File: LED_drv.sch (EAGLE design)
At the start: 69 parts, among them IC1 LM3409, IC2 LM393D, Q2 IPD50R380, T1 IRLR9343PBF, T2 BCX56, T4 BT169, T5 BT169, T6 TLP266J

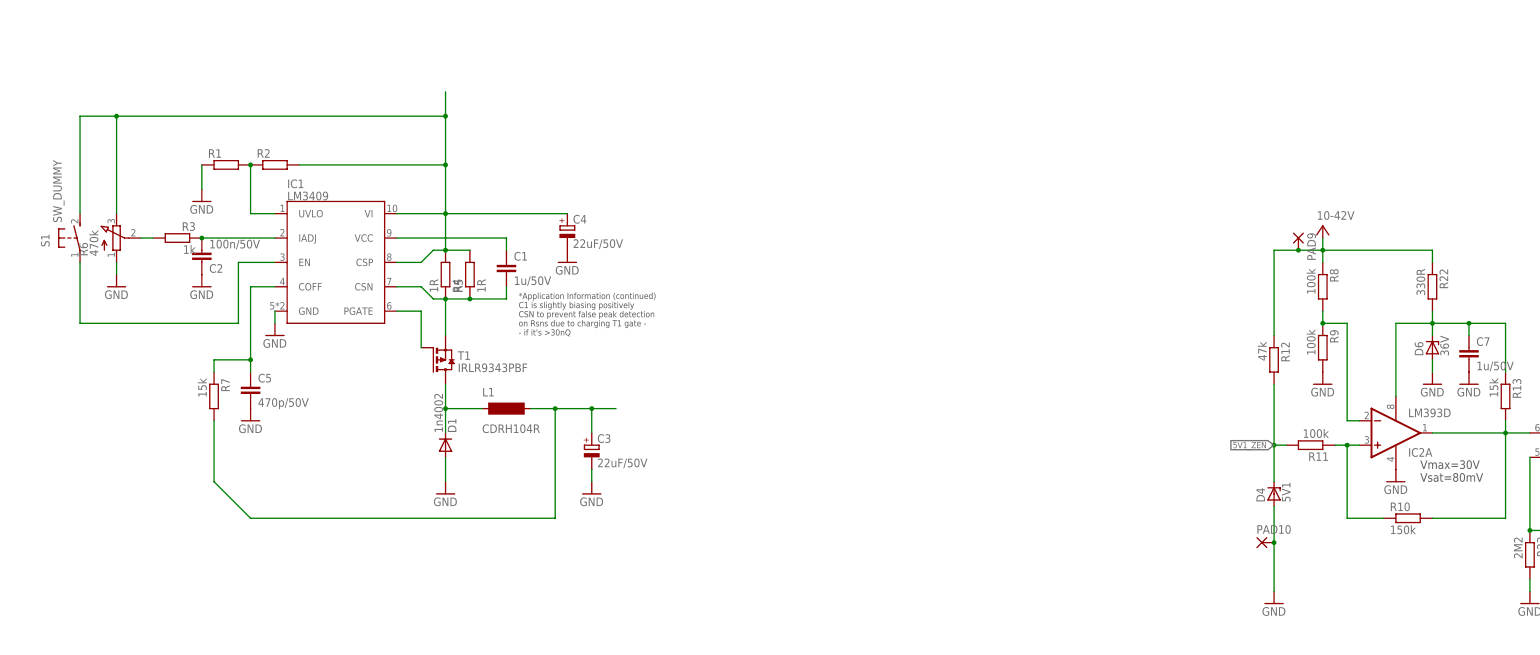
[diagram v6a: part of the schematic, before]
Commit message: PCB layout complete
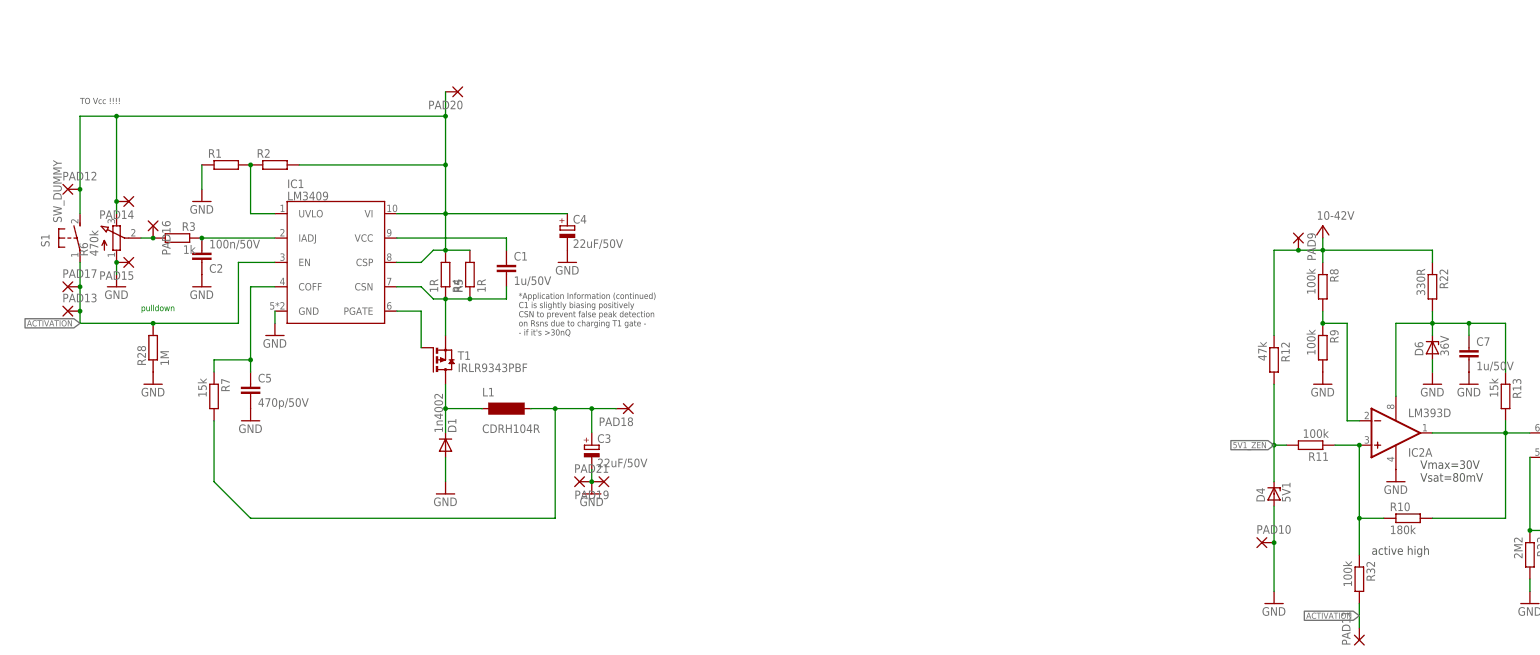
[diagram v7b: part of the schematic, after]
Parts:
- added PAD11, PAD12, PAD13, PAD14, PAD15, PAD16, PAD17, PAD18, PAD19, PAD20, PAD21: (no value), wirepad:SMD2
- added R28: 1M, rcl:R-EU_R0805
- added R32: 100k, resistor:R-EU_R0805
- R1, R2, R7: device rcl:R-EU_R0805 -> rcl:R-EU_R1206
- R10: value 150k -> 180k; device resistor:R-EU_R0805 -> rcl:R-EU_R1206
- R27, R9: device resistor:R-EU_R0805 -> rcl:R-EU_R1206
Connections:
- removed net N$11: IC1.EN, S1.P
- removed net N$20: IC2A.+IN, R10.1, R11.1
- new net ACTIVATION: IC1.EN, PAD11.P, PAD13.P, PAD17.P, R28.2, R32.2, S1.P
- new net EER: IC2A.+IN, R10.1, R11.1, R32.1
- net GND: now also PAD15.P, PAD19.P, PAD21.P, R28.1
- net N$10: now also PAD18.P
- net N$2: now also PAD12.P, PAD14.P, PAD20.P
- net N$8: now also PAD16.P
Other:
- note added: "TO Vcc !!!!"
- note added: "active high"
- note added: "pulldown"
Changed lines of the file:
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@@
 <parts>
 <part name="IC1" library="TI" deviceset="LM3409" device=""/>
-<part name="R1" library="rcl" deviceset="R-EU_" device="R0805"/>
-<part name="R2" library="rcl" deviceset="R-EU_" device="R0805"/>
+<part name="R1" library="rcl" deviceset="R-EU_" device="R1206"/>
+<part name="R2" library="rcl" deviceset="R-EU_" device="R1206"/>
 <part name="GND1" library="supply1" deviceset="GND" device=""/>
 <part name="GND2" library="supply1" deviceset="GND" device=""/>
@@
 <part name="S1" library="switch-omron" deviceset="SW_DUMMY" device=""/>
 <part name="C5" library="rcl" deviceset="C-EU" device="C1206" value="470p/50V"/>
-<part name="R7" library="rcl" deviceset="R-EU_" device="R0805" value="15k"/>
+<part name="R7" library="rcl" deviceset="R-EU_" device="R1206" value="15k"/>
 <part name="GND8" library="supply1" deviceset="GND" device=""/>
 <part name="IC2" library="linear" deviceset="LM393" device="D"/>
 <part name="R8" library="resistor" deviceset="R-EU_" device="R0805" value="100k"/>
-<part name="R9" library="resistor" deviceset="R-EU_" device="R0805" value="100k"/>
-<part name="R10" library="resistor" deviceset="R-EU_" device="R0805" value="150k"/>
+<part name="R9" library="rcl" deviceset="R-EU_" device="R1206" value="100k"/>
+<part name="R10" library="rcl" deviceset="R-EU_" device="R1206" value="180k"/>
 <part name="R11" library="resistor" deviceset="R-EU_" device="R0805" value="100k"/>
 <part name="R12" library="resistor" deviceset="R-EU_" device="R0805" value="47k"/>
@@
 <part name="PAD9" library="wirepad" deviceset="SMD2" device=""/>
 <part name="PAD10" library="wirepad" deviceset="SMD2" device=""/>
-<part name="R27" library="resistor" deviceset="R-EU_" device="R0805" value="0"/>
+<part name="R27" library="rcl" deviceset="R-EU_" device="R1206" value="0"/>
+<part name="R28" library="rcl" deviceset="R-EU_" device="R0805" value="1M"/>
+<part name="GND16" library="supply1" deviceset="GND" device=""/>
+<part name="PAD11" library="wirepad" deviceset="SMD2" device=""/>
+<part name="R32" library="resistor" deviceset="R-EU_" device="R0805" value="100k"/>
+<part name="PAD12" library="wirepad" deviceset="SMD2" device=""/>
+<part name="PAD13" library="wirepad" deviceset="SMD2" device=""/>
+<part name="PAD14" library="wirepad" deviceset="SMD2" device=""/>
+<part name="PAD15" library="wirepad" deviceset="SMD2" device=""/>
+<part name="PAD16" library="wirepad" deviceset="SMD2" device=""/>
+<part name="PAD17" library="wirepad" deviceset="SMD2" device=""/>
+<part name="PAD18" library="wirepad" deviceset="SMD2" device=""/>
+<part name="PAD19" library="wirepad" deviceset="SMD2" device=""/>
+<part name="PAD20" library="wirepad" deviceset="SMD2" device=""/>
+<part name="PAD21" library="wirepad" deviceset="SMD2" device=""/>
 </parts>
 <sheets>
@@
 upewnic wylaczenie MOSa</text>
 <text x="309.88" y="38.1" size="1.778" layer="91">podlacz do zasilacza w srodku</text>
+<text x="243.84" y="-35.56" size="1.778" layer="97">active high</text>
+<text x="-25.4" y="58.42" size="1.27" layer="97">TO Vcc !!!!</text>
+<text x="-12.7" y="15.24" size="1.27" layer="91">pulldown</text>
 </plain>
 <instances>
@@
 <instance part="PAD10" gate="1" x="220.98" y="-33.02"/>
 <instance part="R27" gate="G$1" x="317.5" y="-33.02" rot="R270"/>
+<instance part="R28" gate="G$1" x="-10.16" y="7.62" rot="R90"/>
+<instance part="GND16" gate="1" x="-10.16" y="0"/>
+<instance part="PAD11" gate="1" x="241.3" y="-53.34" rot="R90"/>
+<instance part="R32" gate="G$1" x="241.3" y="-40.64" rot="R270"/>
+<instance part="PAD12" gate="1" x="-27.94" y="40.64"/>
+<instance part="PAD13" gate="1" x="-27.94" y="15.24"/>
+<instance part="PAD14" gate="1" x="-15.24" y="38.1" rot="R180"/>
+<instance part="PAD15" gate="1" x="-15.24" y="25.4" rot="R180"/>
+<instance part="PAD16" gate="1" x="-10.16" y="33.02" rot="R270"/>
+<instance part="PAD17" gate="1" x="-27.94" y="20.32"/>
+<instance part="PAD18" gate="1" x="88.9" y="-5.08" rot="R180"/>
+<instance part="PAD19" gate="1" x="83.82" y="-20.32" rot="R180"/>
+<instance part="PAD20" gate="1" x="53.34" y="60.96" rot="R180"/>
+<instance part="PAD21" gate="1" x="78.74" y="-20.32"/>
 </instances>
 <busses>
@@
 <wire x1="50.8" y1="35.56" x2="76.2" y2="35.56" width="0.1524" layer="91"/>
 <pinref part="R6" gate="G$1" pin="E"/>
-<wire x1="-17.78" y1="35.56" x2="-17.78" y2="55.88" width="0.1524" layer="91"/>
+<wire x1="-17.78" y1="35.56" x2="-17.78" y2="38.1" width="0.1524" layer="91"/>
+<wire x1="-17.78" y1="38.1" x2="-17.78" y2="55.88" width="0.1524" layer="91"/>
 <wire x1="-17.78" y1="55.88" x2="50.8" y2="55.88" width="0.1524" layer="91"/>
 <wire x1="50.8" y1="55.88" x2="50.8" y2="45.72" width="0.1524" layer="91"/>
@@
 <junction x="50.8" y="55.88"/>
 <pinref part="S1" gate="G$1" pin="S"/>
-<wire x1="-25.4" y1="35.56" x2="-25.4" y2="55.88" width="0.1524" layer="91"/>
+<wire x1="-25.4" y1="35.56" x2="-25.4" y2="40.64" width="0.1524" layer="91"/>
+<wire x1="-25.4" y1="40.64" x2="-25.4" y2="55.88" width="0.1524" layer="91"/>
 <wire x1="-25.4" y1="55.88" x2="-17.78" y2="55.88" width="0.1524" layer="91"/>
 <junction x="-17.78" y="55.88"/>
+<pinref part="PAD12" gate="1" pin="P"/>
+<junction x="-25.4" y="40.64"/>
+<pinref part="PAD14" gate="1" pin="P"/>
+<junction x="-17.78" y="38.1"/>
+<pinref part="PAD20" gate="1" pin="P"/>
 </segment>
 </net>
@@
 <pinref part="C3" gate="G$1" pin="-"/>
 <wire x1="81.28" y1="-20.32" x2="81.28" y2="-17.78" width="0.1524" layer="91"/>
+<pinref part="PAD19" gate="1" pin="P"/>
+<junction x="81.28" y="-20.32"/>
+<pinref part="PAD21" gate="1" pin="P"/>
 </segment>
 <segment>
@@
 <pinref part="R6" gate="G$1" pin="A"/>
 <pinref part="GND7" gate="1" pin="GND"/>
-<wire x1="-17.78" y1="22.86" x2="-17.78" y2="25.4" width="0.1524" layer="91"/>
+<pinref part="PAD15" gate="1" pin="P"/>
+<junction x="-17.78" y="25.4"/>
+<wire x1="-17.78" y1="25.4" x2="-17.78" y2="22.86" width="0.1524" layer="91"/>
 </segment>
 <segment>
@@
 <pinref part="GND15" gate="1" pin="GND"/>
 <wire x1="289.56" y1="20.32" x2="289.56" y2="15.24" width="0.1524" layer="91"/>
+</segment>
+<segment>
+<pinref part="R28" gate="G$1" pin="1"/>
+<pinref part="GND16" gate="1" pin="GND"/>
 </segment>
 </net>
@@
 <wire x1="73.66" y1="-27.94" x2="73.66" y2="-5.08" width="0.1524" layer="91"/>
 <junction x="73.66" y="-5.08"/>
+<pinref part="PAD18" gate="1" pin="P"/>
 </segment>
 </net>
@@
 <pinref part="R3" gate="G$1" pin="2"/>
 <wire x1="-12.7" y1="30.48" x2="-10.16" y2="30.48" width="0.1524" layer="91"/>
-</segment>
-</net>
-<net name="N$11" class="0">
-<segment>
-<pinref part="IC1" gate="G$1" pin="EN"/>
-<wire x1="15.24" y1="25.4" x2="7.62" y2="25.4" width="0.1524" layer="91"/>
-<wire x1="7.62" y1="25.4" x2="7.62" y2="12.7" width="0.1524" layer="91"/>
-<wire x1="7.62" y1="12.7" x2="-25.4" y2="12.7" width="0.1524" layer="91"/>
-<wire x1="-25.4" y1="12.7" x2="-25.4" y2="25.4" width="0.1524" layer="91"/>
-<pinref part="S1" gate="G$1" pin="P"/>
+<pinref part="PAD16" gate="1" pin="P"/>
+<junction x="-10.16" y="30.48"/>
 </segment>
 </net>
@@
 </segment>
 </net>
-<net name="N$20" class="0">
-<segment>
-<pinref part="R10" gate="G$1" pin="1"/>
-<wire x1="246.38" y1="-27.94" x2="238.76" y2="-27.94" width="0.1524" layer="91"/>
-<pinref part="R11" gate="G$1" pin="1"/>
-<pinref part="IC2" gate="A" pin="+IN"/>
-<wire x1="241.3" y1="-12.7" x2="238.76" y2="-12.7" width="0.1524" layer="91"/>
-<wire x1="238.76" y1="-12.7" x2="236.22" y2="-12.7" width="0.1524" layer="91"/>
-<wire x1="238.76" y1="-27.94" x2="238.76" y2="-12.7" width="0.1524" layer="91"/>
-<junction x="238.76" y="-12.7"/>
+<net name="ACTIVATION" class="0">
+<segment>
+<pinref part="IC1" gate="G$1" pin="EN"/>
+<wire x1="15.24" y1="25.4" x2="7.62" y2="25.4" width="0.1524" layer="91"/>
+<wire x1="7.62" y1="25.4" x2="7.62" y2="12.7" width="0.1524" layer="91"/>
+<wire x1="7.62" y1="12.7" x2="-10.16" y2="12.7" width="0.1524" layer="91"/>
+<wire x1="-10.16" y1="12.7" x2="-25.4" y2="12.7" width="0.1524" layer="91"/>
+<wire x1="-25.4" y1="12.7" x2="-25.4" y2="15.24" width="0.1524" layer="91"/>
+<pinref part="S1" gate="G$1" pin="P"/>
+<label x="-25.4" y="12.7" size="1.27" layer="95" rot="R180" xref="yes"/>
+<pinref part="R28" gate="G$1" pin="2"/>
+<junction x="-10.16" y="12.7"/>
+<pinref part="PAD13" gate="1" pin="P"/>
+<wire x1="-25.4" y1="15.24" x2="-25.4" y2="20.32" width="0.1524" layer="91"/>
+<junction x="-25.4" y="15.24"/>
+<pinref part="PAD17" gate="1" pin="P"/>
+<wire x1="-25.4" y1="20.32" x2="-25.4" y2="25.4" width="0.1524" layer="91"/>
+<junction x="-25.4" y="20.32"/>
+</segment>
+<segment>
+<pinref part="R32" gate="G$1" pin="2"/>
+<wire x1="241.3" y1="-50.8" x2="241.3" y2="-45.72" width="0.1524" layer="91"/>
+<pinref part="PAD11" gate="1" pin="P"/>
+<label x="241.3" y="-48.26" size="1.27" layer="95" rot="R180" xref="yes"/>
 </segment>
 </net>
@@
 </segment>
 </net>
+<net name="EER" class="0">
+<segment>
+<pinref part="R11" gate="G$1" pin="1"/>
+<pinref part="IC2" gate="A" pin="+IN"/>
+<junction x="241.3" y="-12.7"/>
+<wire x1="241.3" y1="-12.7" x2="236.22" y2="-12.7" width="0.1524" layer="91"/>
+<pinref part="R32" gate="G$1" pin="1"/>
+<wire x1="241.3" y1="-35.56" x2="241.3" y2="-27.94" width="0.1524" layer="91"/>
+<pinref part="R10" gate="G$1" pin="1"/>
+<wire x1="241.3" y1="-27.94" x2="241.3" y2="-12.7" width="0.1524" layer="91"/>
+<wire x1="246.38" y1="-27.94" x2="241.3" y2="-27.94" width="0.1524" layer="91"/>
+<junction x="241.3" y="-27.94"/>
+</segment>
+</net>

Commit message: PCB layout complete
minor update
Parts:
- removed C4: 22uF/50V, rcl:CPOL-EUE5-6
- removed C6: 100n/400V, rcl:C-US075-032X103
- added 0R, R31, R33, R34, R35, R36: 1R, resistor:R-EU_R1206
- added C12, C13: 22uF/50V, rcl:CPOL-EUE5-6
- added F1: (no value), fuse:SH22,5A
- added PAD22, PAD23, PAD24, PAD25, PAD26, PAD27, PAD28, PAD29: (no value), wirepad:SMD2
- added R37: S14K275_SMD, varistor:S14K275_SMD
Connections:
- new net 230VAC(N/L)_IN: F1.2
- new net N$11: C13.+, C3.+, L1.2, R31.2, R33.2, R34.2, R35.2, R36.2, R7.2
- new net N$20: PAD22.P, R33.1
- new net N$32: PAD18.P, R31.1
- new net N$35: PAD23.P, R34.1
- new net N$36: PAD24.P, R35.1
- new net N$37: PAD25.P, R36.1
- net 230VAC(L/N): now also R37.2
- net 230VAC(N/L): now also F1.1, R37.1
- net ACTIVATION: now also 0R.1; no longer PAD17.P, S1.P
- net GND: now also C12.-, C13.-, PAD26.P, PAD27.P, PAD28.P, PAD29.P; no longer C4.-
- net N$10: now also 0R.2, PAD17.P, S1.P; no longer C3.+, L1.2, PAD18.P, R7.2
- net N$14: no longer C6.1
- net N$2: now also C12.+; no longer C4.+
- net N$34: no longer C6.2
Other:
- moved on the sheet: C10, C11, C8, PAD1, PAD13, PAD17, PAD18, PAD19, PAD2, PAD20, PAD21, R28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
